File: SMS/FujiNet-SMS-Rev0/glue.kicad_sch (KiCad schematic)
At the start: 12 parts, among them U4 74HCT14, U5 74HCT27, U6 74HCT27, U7 74HCT10, U8 74HCT00

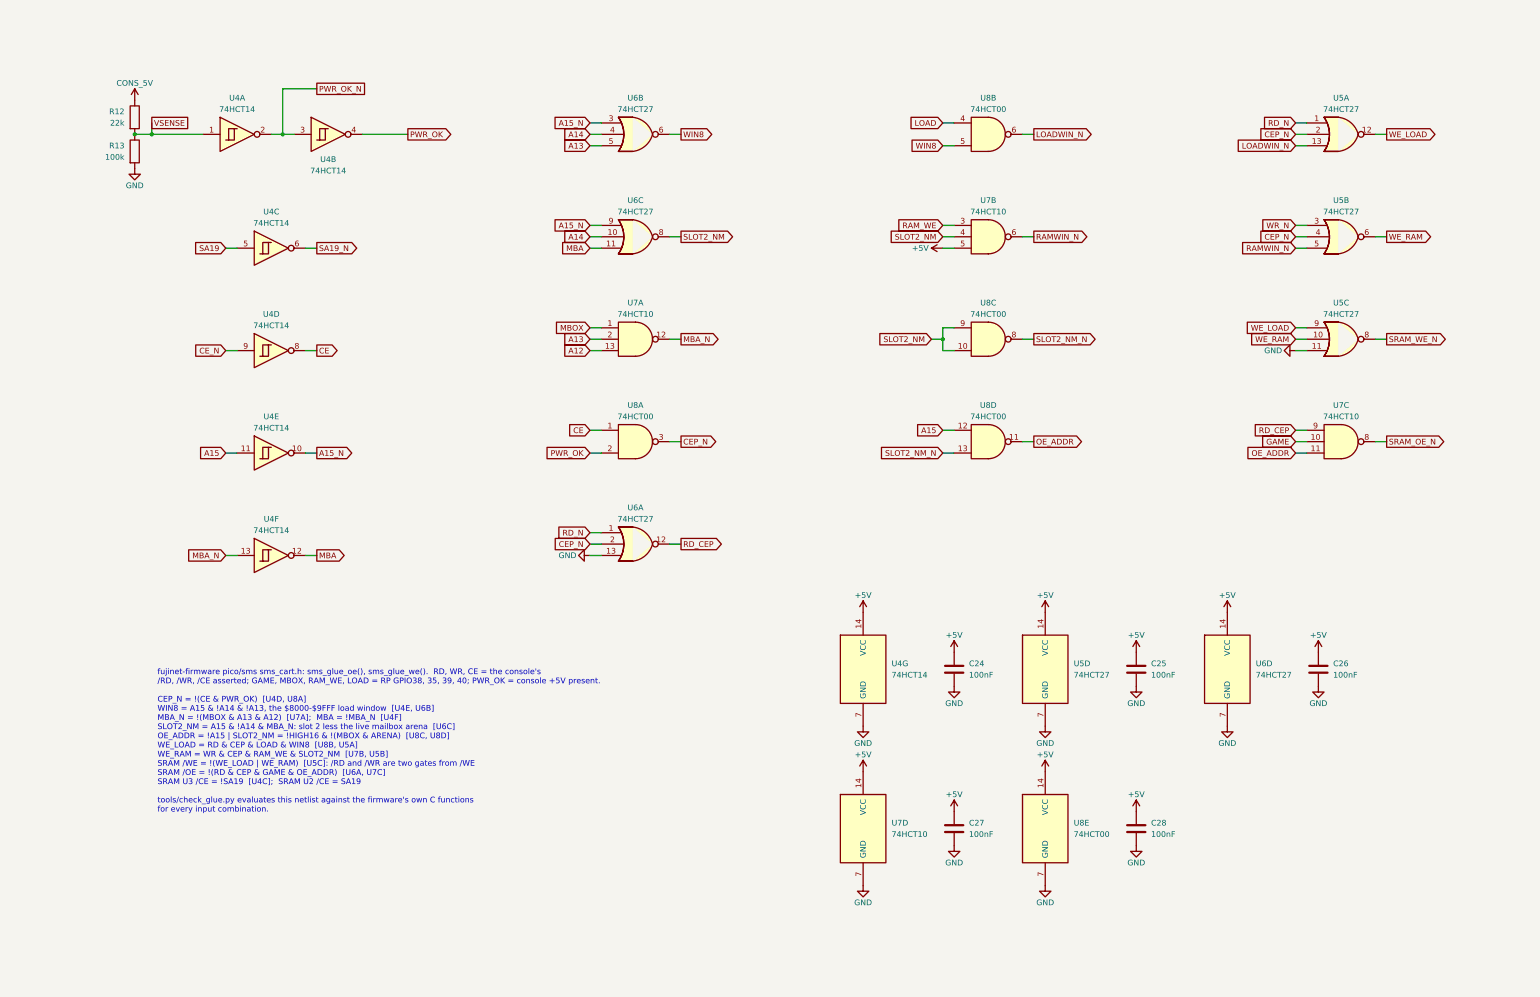
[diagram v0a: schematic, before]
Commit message: SMS Rev0: audit with kicad-happy + datasheets, fix the edge, redraw the schematic
Edge connector: every source (SMS Power slot diagram, little-scale, a 171-5519
scan, raphnet, the barbeque and reidrac footprints) puts the EVEN pins on the
component / label side with pins 1/2 at the right.  The schematic-only
footprint had the faces swapped, which would have put console +5V on /WR.
make_edge_fp.py now writes even pads on F.Cu, odd on B.Cu, 1.75 x 8.75 mm
fingers 0.75-9.5 mm from the edge on a 65.8 mm tab; check_nets.py asserts it
and tools/audit/edge_orientation.py checks it against the sources.

kicad-happy + datasheet audit (docs/design-review-rev0.md Part 1, 27 deep
review findings, gate 27/27): R_VBPD 4.7k VBUS pull-down (SS34 leakage lifts
the P-FET gate), /WAIT gate pull-up 10k -> 4.7k (GPIO34's reset pull-down vs
the 2N7002's 2.5 V threshold), 10 uF bulk on the console 5V.

Schematic: hierarchical sheets wired on a root block diagram (edge -> RP2354B
-> ESP32-S3 -> USB, glue and SRAM under the RP, power below); every sheet
drawn left to right, the glue as a wired logic network by gate depth, the
RP2354B mirrored so its bus faces the console, small sheets on A4.  Parts
are addressed by key (design.py), no more NES reference aliasing.  sch_draw
gains hierarchical labels, sheet blocks, a bus graph and flag / power-pin
lints; gen_sch checks the hierarchy against design.py and names nets by
their last path element (one bus vector per bus: KiCad joins differing
vectors by position).  ERC 0, check_nets 437/437, check_glue 8192/8192.

JLC CPL rotations measured against the EasyEDA footprint of every LCSC part
(tools/audit/jlc); the AS6C4008 has no EasyEDA footprint.

Co-Authored-By: Claude Opus 5.5 <noreply@anthropic.com>
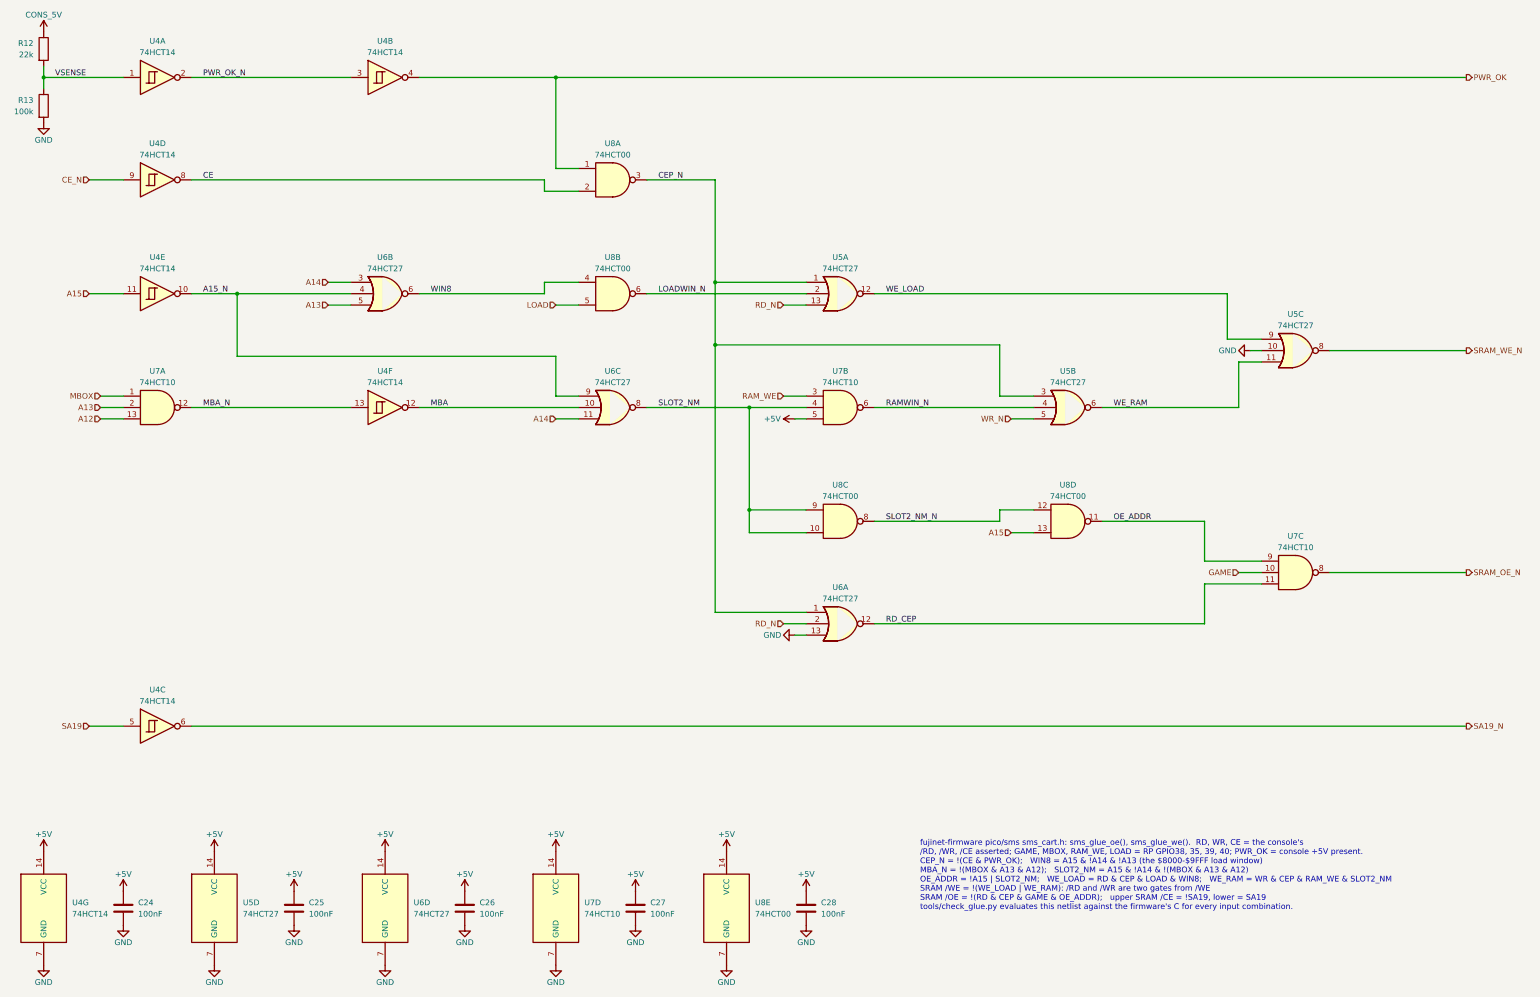
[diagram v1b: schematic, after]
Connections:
- net A14: now also U6.11, U6.3; no longer U6.10, U6.4
- net A15: now also U8.13; no longer U8.12
- net A15_N: now also U6.4; no longer U6.3
- net CE: now also U8.2; no longer U8.1
- net CEP_N: now also U5.1, U5.3, U6.1; no longer U5.2, U5.4, U6.2
- net GND: now also U5.10; no longer U5.11
- net LOAD: now also U8.5; no longer U8.4
- net LOADWIN_N: now also U5.2; no longer U5.13
- net MBA: now also U6.10; no longer U6.11
- net OE_ADDR: now also U7.9; no longer U7.11
- net PWR_OK: now also U8.1; no longer U8.2
- net RAMWIN_N: now also U5.4; no longer U5.5
- net RD_CEP: now also U7.11; no longer U7.9
- net RD_N: now also U5.13, U6.2; no longer U5.1, U6.1
- net SLOT2_NM_N: now also U8.12; no longer U8.13
- net WE_RAM: now also U5.11; no longer U5.10
- net WIN8: now also U8.4; no longer U8.5
- net WR_N: now also U5.5; no longer U5.3
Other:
- note added: "fujinet-firmware pico/sms sms_cart.h: sms_glue_oe(), sms_glue_we(). RD, WR, CE = the console's /RD, /WR, /CE asserted; GAME, MBOX, RAM_WE, LOAD = RP GPIO38, 35, 39, 40; PWR_OK = console +5V present. CEP_N = !(CE & PWR_OK); WIN8 = A15 & !A14 & !A13 (the $8000-$9FFF load window) MBA_N = !(MBOX & A13 & A12); SLOT2_NM = A15 & !A14 & !(MBOX & A13 & A12) OE_ADDR = !A15 | SLOT2_NM; WE_LOAD = RD & CEP & 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"
- note removed: "fujinet-firmware pico/sms sms_cart.h: sms_glue_oe(), sms_glue_we(). RD, WR, CE = the console's /RD, /WR, /CE asserted; GAME, MBOX, RAM_WE, LOAD = RP GPIO38, 35, 39, 40; PWR_OK = console +5V present. CEP_N = !(CE & PWR_OK) [U4D, U8A] WIN8 = A15 & !A14 & !A13, the $8000-$9FFF load window [U4E, U6B] MBA_N = !(MBOX & A13 & A12) [U7A]; MBA = !MBA_N [U4F] SLOT2_NM = A15 & !A14 & MBA_N: slot 2 less the 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"
- moved on the sheet: C24, C25, C26, C27, C28, R12, R13, U4A, U4B, U4C, U4D, U4E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

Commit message: SMS Rev0 v2: port the FujiNet-7800 tooling, swap the near-stock-out parts
- export.py: JLCPCB and PCBWay packages (PCBWay turnkey BOM, centroid,
  assembly drawing); Manufacturer on every BOM part (design.MFR), written
  to symbols and footprints alike
- edge_geom.py: the SMS edge constants in one place (make_edge_fp,
  gen_pcb, check_gerbers); gen_pcb's body height, holes and In4 split now
  come from placement.py
- footprint paths from the schematic netlist (gen_pcb.fp_sheet_unit), so
  a part's units can be drawn on several sheets (prototype 2026-10-08:
  kicad-cli files it under the first sheet, parity accepts it)
- check_vias, check_gerbers, make_happy_config, stitch_gnd second ring,
  set_models main(), route_board.sh 12 passes / hybrid, DRC at all
  severities
- TL3342 -> TS-1187A-B-A-B (C318884), WS2812B-2020-V6 -> WS2812C-2020-V1
  (C2976072): ~5 in stock on 2026-10-07

Co-Authored-By: Claude Opus 5.5 <noreply@anthropic.com>
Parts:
- C24, C25, C26, C27, C28: Manufacturer (none) -> YAGEO
- R12, R13: Manufacturer (none) -> UNI-ROYAL
- U4, U8: Manufacturer (none) -> Texas Instruments
- U5, U6, U7: Manufacturer (none) -> Nexperia
